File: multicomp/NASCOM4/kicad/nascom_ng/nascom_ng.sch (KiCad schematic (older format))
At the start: 22 parts, among them J11 Conn_02x08_Odd_Even, J6 Conn_02x14_Even_Odd, J7 Conn_02x14_Even_Odd, J8 Conn_02x14_Even_Odd, J9 Conn_02x14_Even_Odd, SW1 SW_Push, SW2 SW_Push, SW3 SW_Push, X1 NASCOM-logo, X2 KiCad-sm-logo

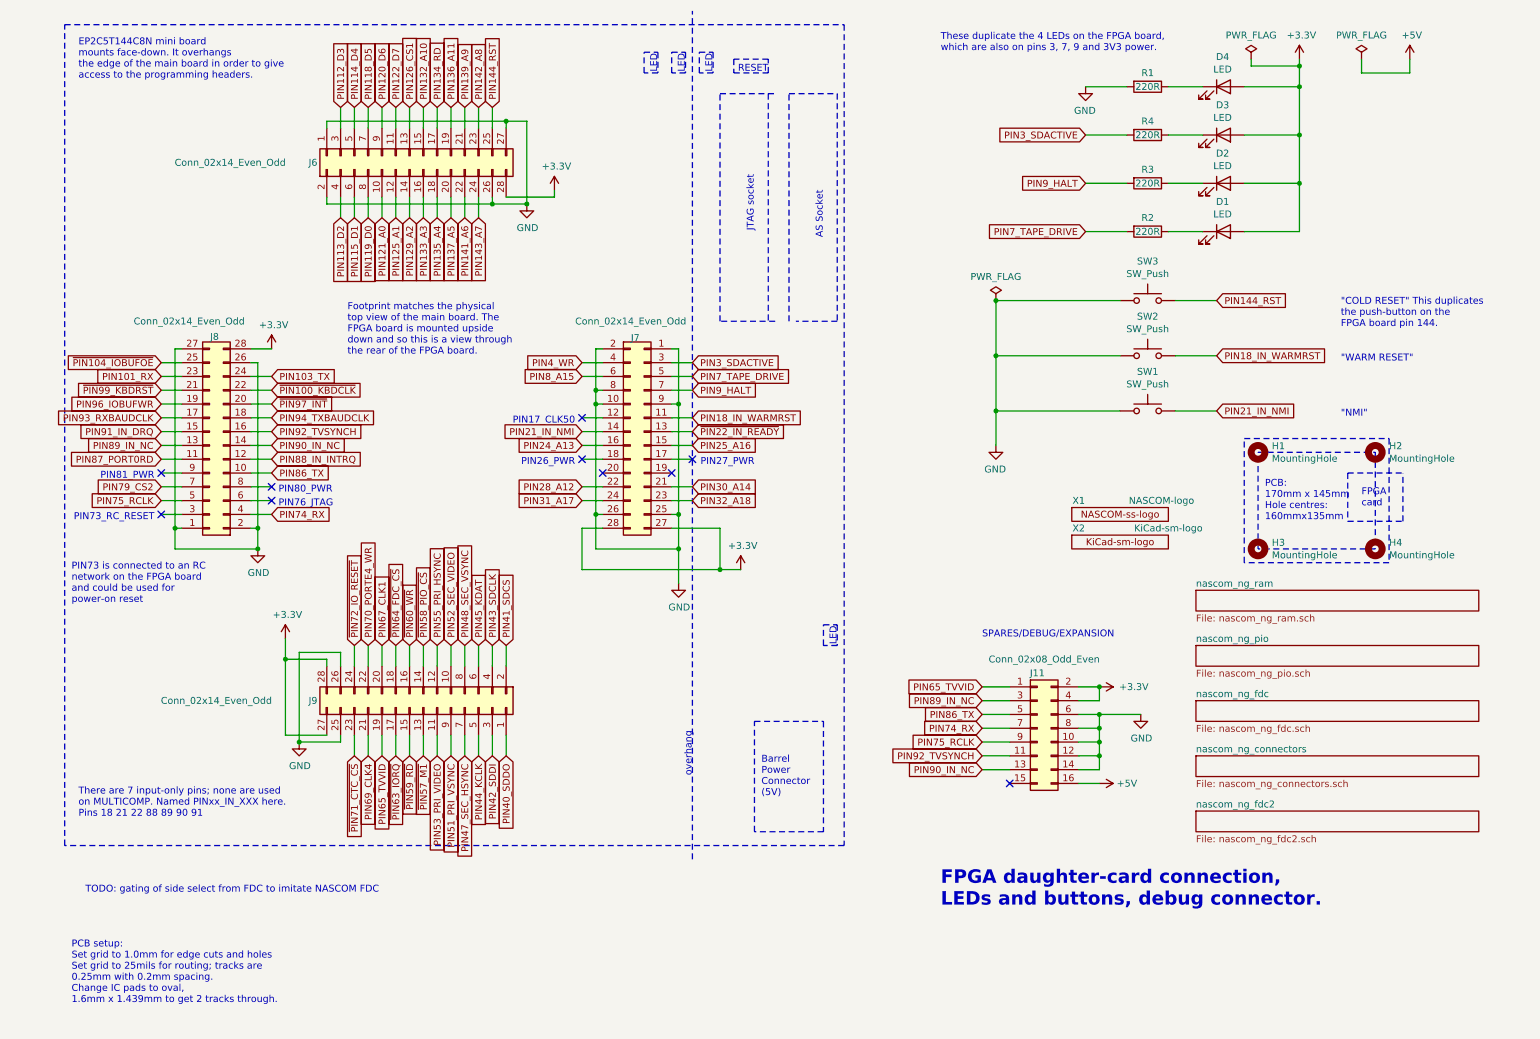
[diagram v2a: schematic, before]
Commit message: Add REVB data-base: schematics, pcb and manufacturing files
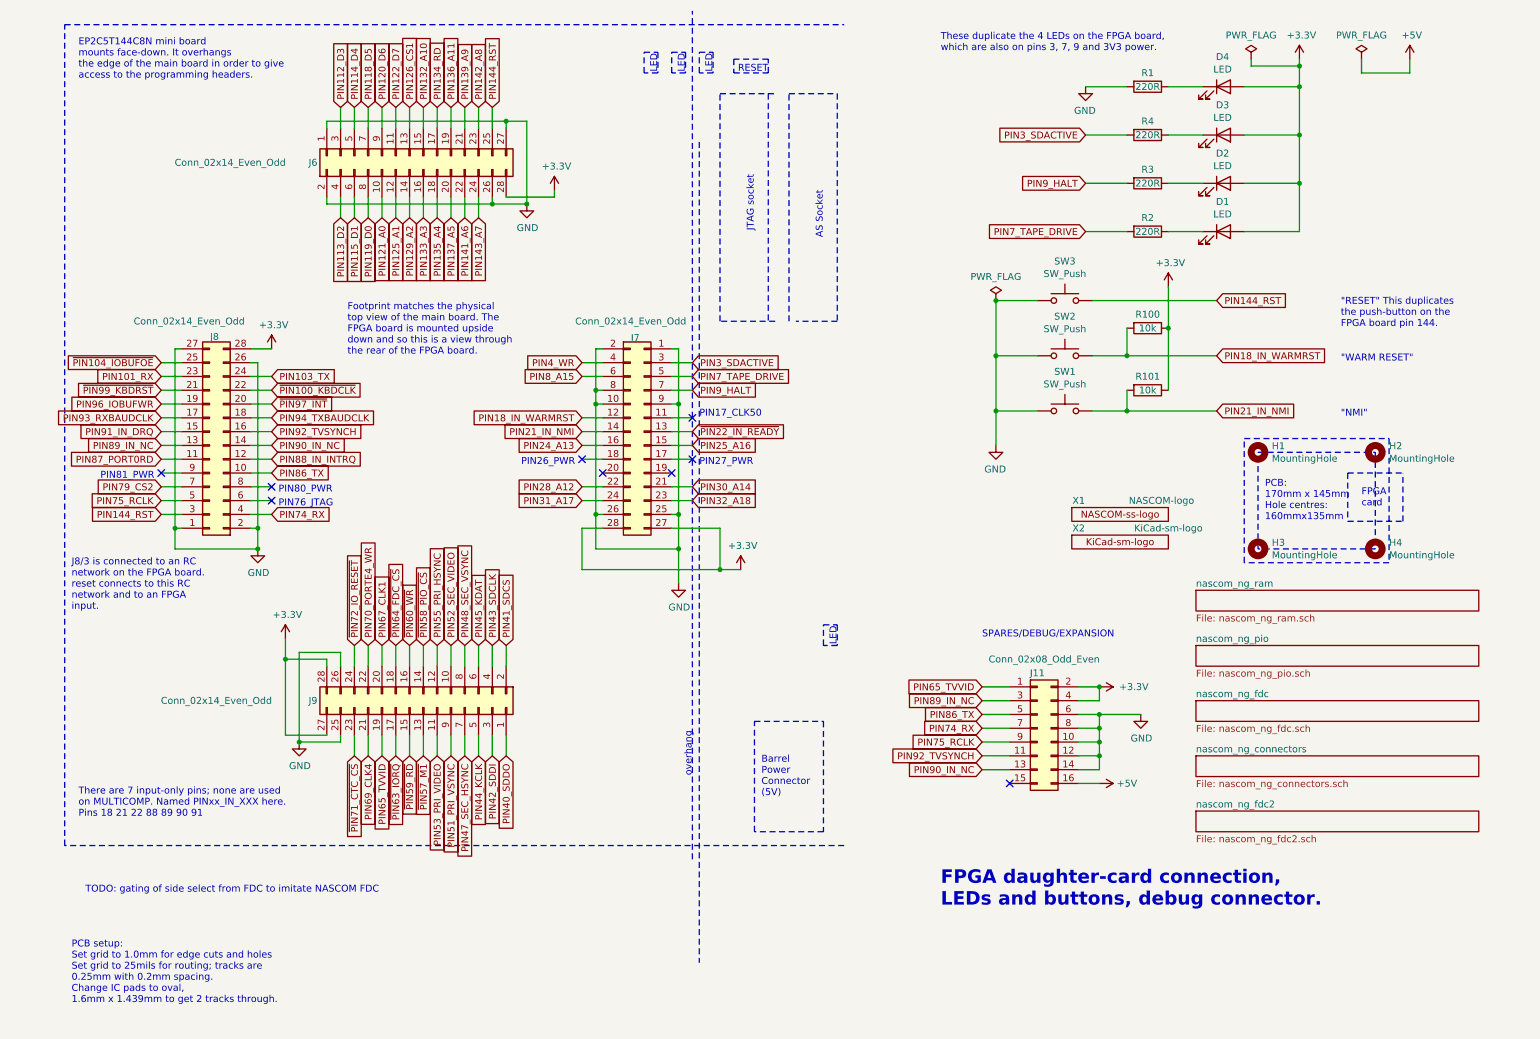
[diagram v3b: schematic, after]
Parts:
- added R100, R101: 10k, Resistor_THT:R_Axial_DIN0204_L3.6mm_D1.6mm_P7.62mm_Horizontal, symbol Device:R
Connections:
- net +3V3: now also R100.1, R101.1
- net PIN144_RST: now also J8.3 (Pin_3)
- net PIN18_IN_WARMRST: now also J7.12 (Pin_12), R100.2; no longer J7.11 (Pin_11)
- net PIN21_IN_NMI: now also R101.2
- no-connect marks 10 -> 9
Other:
- note added: ""RESET" This duplicates\nthe push-button on the\nFPGA board pin 144."
- note added: "J8/3 is connected to an RC\nnetwork on the FPGA board.\nreset connects to this RC\nnetwork and to an FPGA\ninput."
- note removed: ""COLD RESET" This duplicates\nthe push-button on the\nFPGA board pin 144."
- note removed: "PIN73 is connected to an RC\nnetwork on the FPGA board\nand could be used for\npower-on reset"
- note removed: "PIN73_RC_RESET"
- moved on the sheet: SW1, SW2, SW3
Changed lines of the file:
@@
 Sheet 1 6
 Title "NASCOM 4 - a NASCOM in an FPGA"
-Date "14-Feb-2021"
-Rev "A"
+Date "20-Oct-2021"
+Rev "B"
 Comp ""
 Comment1 ""
@@
 Wire Wire Line
 	5200 3400 5350 3400
-Text GLabel 5350 3400 2    50   Input ~ 0
+Text GLabel 4550 3400 0    50   Input ~ 0
 PIN18_IN_WARMRST
 Wire Wire Line
@@
 	800  550  6450 550
 Wire Notes Line
-	6450 550  6450 6500
+	5400 1400 5400 7350
 Wire Notes Line
 	6450 6500 800  6500
@@
 $EndSheet
 Text Notes 10050 2750 0    50   ~ 0
-"COLD RESET" This duplicates\nthe push-button on the\nFPGA board pin 144.
+"RESET" This duplicates\nthe push-button on the\nFPGA board pin 144.
 Text GLabel 1500 3100 0    50   Input ~ 0
 PIN101_RX
@@
 Text Notes 950  6850 0    50   ~ 0
 TODO: gating of side select from FDC to imitate NASCOM FDC\n
-Text Notes 4500 3450 2    50   ~ 0
+Text Notes 5400 3400 0    50   ~ 0
 PIN17_CLK50
-NoConn ~ 4550 3400
-Text Notes 5800 3750 2    50   ~ 0
+NoConn ~ 5350 3400
+Text Notes 5400 3750 0    50   ~ 0
 PIN27_PWR
 NoConn ~ 5350 3700
@@
 PIN81_PWR
 NoConn ~ 1500 3800
-Text Notes 1450 4150 2    50   ~ 0
-PIN73_RC_RESET
-NoConn ~ 1500 4100
 Text Notes 2350 4050 0    50   ~ 0
 PIN76_JTAG
@@
 Text Notes 7150 750  0    50   ~ 0
 These duplicate the 4 LEDs on the FPGA board,\nwhich are also on pins 3, 7, 9 and 3V3 power.
-Text Notes 850  4750 0    50   ~ 0
-PIN73 is connected to an RC\nnetwork on the FPGA board\nand could be used for\npower-on reset
+Text Notes 850  4800 0    50   ~ 0
+J8/3 is connected to an RC\nnetwork on the FPGA board.\nreset connects to this RC\nnetwork and to an FPGA\ninput.
 Text Notes 900  950  0    50   ~ 0
 EP2C5T144C8N mini board\nmounts face-down. It overhangs\nthe edge of the main board in order to give\naccess to the programming headers.
@@
 PIN144_RST
 Wire Wire Line
-	9150 2550 8850 2550
-Wire Wire Line
-	8450 2550 7550 2550
+	9150 2550 8250 2550
+Wire Wire Line
+	7850 2550 7550 2550
 Connection ~ 7550 2550
 Connection ~ 7550 3350
 Wire Wire Line
-	8450 3350 7550 3350
+	7850 3350 7550 3350
 Wire Wire Line
 	7550 2950 7550 3350
 Connection ~ 7550 2950
 Wire Wire Line
-	8450 2950 7550 2950
+	7850 2950 7550 2950
 $Comp
 L power:GND #PWR0122
@@
 Wire Wire Line
 	7550 2550 7550 2950
-Wire Wire Line
-	9150 3350 8850 3350
 Text GLabel 9150 3350 2    50   Input ~ 0
 PIN21_IN_NMI
 Wire Wire Line
-	9150 2950 8850 2950
+	9150 2950 8500 2950
 Text GLabel 9150 2950 2    50   Input ~ 0
 PIN18_IN_WARMRST
@@
 L Switch:SW_Push SW3
 U 1 1 60158A7D
-P 8650 2550
-F 0 "SW3" H 8650 2835 50  0000 C CNN
-F 1 "SW_Push" H 8650 2744 50  0000 C CNN
-F 2 "mylib:MOMENTARY_TACTILE_RT_ANGLE" H 8650 2750 50  0001 C CNN
-F 3 "~" H 8650 2750 50  0001 C CNN
-	1    8650 2550
+P 8050 2550
+F 0 "SW3" H 8050 2835 50  0000 C CNN
+F 1 "SW_Push" H 8050 2744 50  0000 C CNN
+F 2 "mylib:MOMENTARY_TACTILE_RT_ANGLE" H 8050 2750 50  0001 C CNN
+F 3 "~" H 8050 2750 50  0001 C CNN
+	1    8050 2550
 	1    0    0    -1
 $EndComp
@@
 L Switch:SW_Push SW2
 U 1 1 6015E3B1
-P 8650 2950
-F 0 "SW2" H 8650 3235 50  0000 C CNN
-F 1 "SW_Push" H 8650 3144 50  0000 C CNN
-F 2 "mylib:MOMENTARY_TACTILE_RT_ANGLE" H 8650 3150 50  0001 C CNN
-F 3 "~" H 8650 3150 50  0001 C CNN
-	1    8650 2950
+P 8050 2950
+F 0 "SW2" H 8050 3235 50  0000 C CNN
+F 1 "SW_Push" H 8050 3144 50  0000 C CNN
+F 2 "mylib:MOMENTARY_TACTILE_RT_ANGLE" H 8050 3150 50  0001 C CNN
+F 3 "~" H 8050 3150 50  0001 C CNN
+	1    8050 2950
 	1    0    0    -1
 $EndComp
@@
 L Switch:SW_Push SW1
 U 1 1 6015E8F2
-P 8650 3350
-F 0 "SW1" H 8650 3635 50  0000 C CNN
-F 1 "SW_Push" H 8650 3544 50  0000 C CNN
-F 2 "mylib:MOMENTARY_TACTILE_RT_ANGLE" H 8650 3550 50  0001 C CNN
-F 3 "~" H 8650 3550 50  0001 C CNN
-	1    8650 3350
+P 8050 3350
+F 0 "SW1" H 8050 3635 50  0000 C CNN
+F 1 "SW_Push" H 8050 3544 50  0000 C CNN
+F 2 "mylib:MOMENTARY_TACTILE_RT_ANGLE" H 8050 3550 50  0001 C CNN
+F 3 "~" H 8050 3550 50  0001 C CNN
+	1    8050 3350
 	1    0    0    -1
 $EndComp
@@
 Text Notes 850  7650 0    50   ~ 0
 PCB setup:\nSet grid to 1.0mm for edge cuts and holes\nSet grid to 25mils for routing; tracks are\n0.25mm with 0.2mm spacing.\nChange IC pads to oval,\n1.6mm x 1.439mm to get 2 tracks through.
+Text GLabel 1500 4100 0    50   Input ~ 0
+PIN144_RST
+$Comp
+L Device:R R100
+U 1 1 617B2C8D
+P 8650 2750
+F 0 "R100" V 8550 2750 50  0000 C CNN
+F 1 "10k" V 8650 2750 50  0000 C CNN
+F 2 "Resistor_THT:R_Axial_DIN0204_L3.6mm_D1.6mm_P7.62mm_Horizontal" V 8580 2750 50  0001 C CNN
+F 3 "~" H 8650 2750 50  0001 C CNN
+	1    8650 2750
+	0    1    1    0
+$EndComp
+$Comp
+L Device:R R101
+U 1 1 617B3178
+P 8650 3200
+F 0 "R101" V 8550 3200 50  0000 C CNN
+F 1 "10k" V 8650 3200 50  0000 C CNN
+F 2 "Resistor_THT:R_Axial_DIN0204_L3.6mm_D1.6mm_P7.62mm_Horizontal" V 8580 3200 50  0001 C CNN
+F 3 "~" H 8650 3200 50  0001 C CNN
+	1    8650 3200
+	0    1    1    0
+$EndComp
+Wire Wire Line
+	8500 2750 8500 2950
+Connection ~ 8500 2950
+Wire Wire Line
+	8500 2950 8250 2950
+Wire Wire Line
+	8500 3200 8500 3350
+Wire Wire Line
+	8250 3350 8500 3350
+Connection ~ 8500 3350
+Wire Wire Line
+	8500 3350 9150 3350
+Wire Wire Line
+	8800 3200 8800 2750
+$Comp
+L power:+3.3V #PWR0143
+U 1 1 617D0C44
+P 8800 2450
+F 0 "#PWR0143" H 8800 2300 50  0001 C CNN
+F 1 "+3.3V" H 8815 2623 50  0000 C CNN
+F 2 "" H 8800 2450 50  0001 C CNN
+F 3 "" H 8800 2450 50  0001 C CNN
+	1    8800 2450
+	1    0    0    -1
+$EndComp
+Wire Wire Line
+	8800 2450 8800 2750
+Connection ~ 8800 2750
 $EndSCHEMATC
